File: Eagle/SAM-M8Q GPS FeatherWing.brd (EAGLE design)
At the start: 50.8 x 22.9 mm, 25 parts, among them Q1 DMG3415U-7, Q2 2N2222, SW1 KMR2, U1 SAM-M8Q

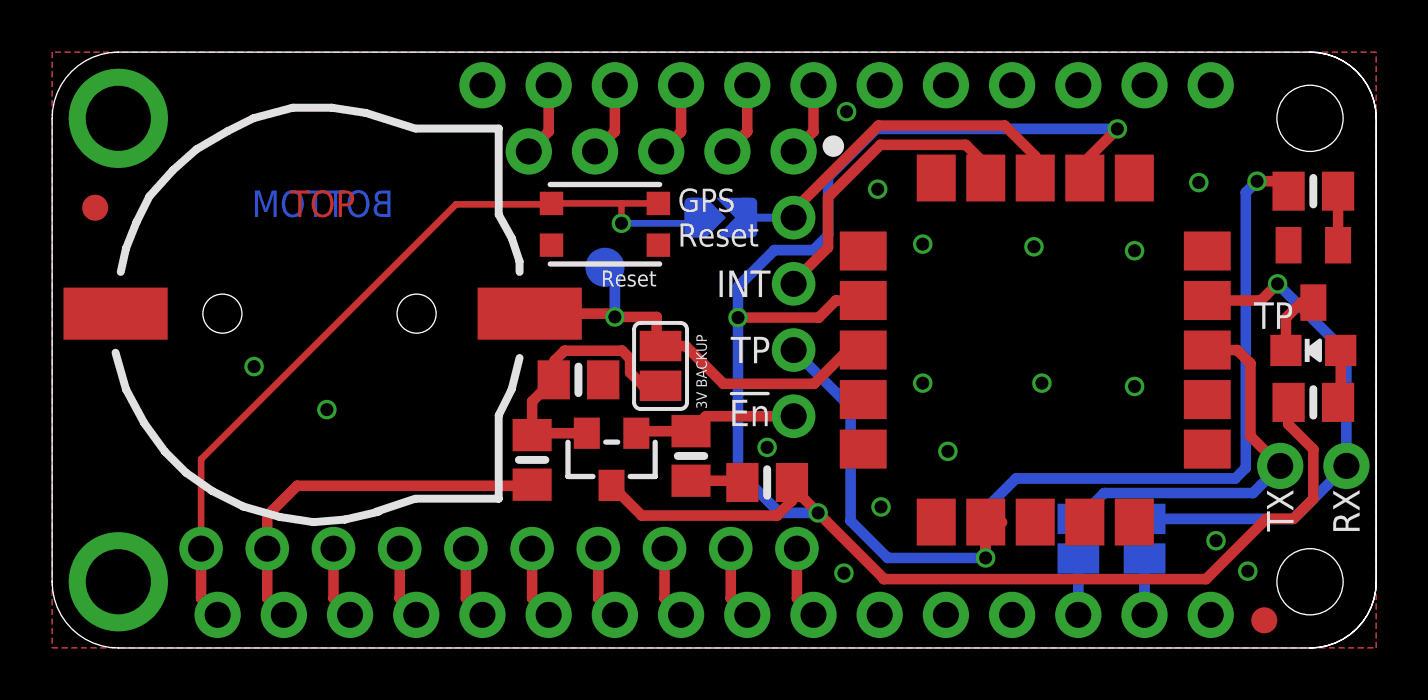
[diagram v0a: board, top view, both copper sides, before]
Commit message: Reduced vias. Added pad for SAFEBOOT.
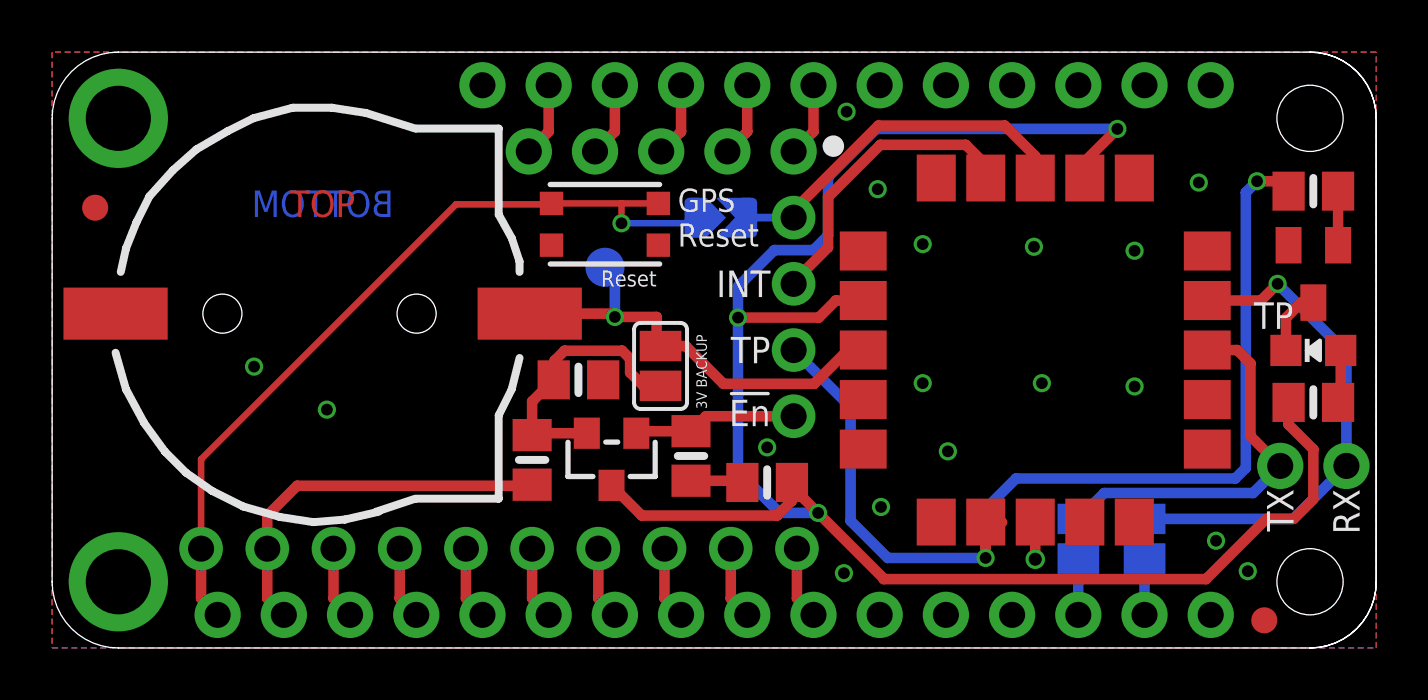
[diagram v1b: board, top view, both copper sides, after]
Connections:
- new net SAFEBOOT: U1.8
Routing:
- net SAFEBOOT: track 0.00 -> 1.43 mm, vias 0 -> 1
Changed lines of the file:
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@@
 <text x="38.1" y="18.034" size="1.6764" layer="22" font="vector" ratio="15" rot="MR0" align="center">SAM-M8Q GPS
 FeatherWing</text>
-<text x="43.688" y="4.191" size="1.016" layer="22" font="vector" ratio="14" rot="MR270" align="center">RX</text>
-<text x="37.465" y="4.191" size="1.016" layer="22" font="vector" ratio="14" rot="MR270" align="center">TX</text>
+<text x="43.7134" y="4.953" size="1.016" layer="22" font="vector" ratio="14" rot="MR270" align="center">RX</text>
+<text x="37.5666" y="4.953" size="1.016" layer="22" font="vector" ratio="14" rot="MR270" align="center">TX</text>
 <text x="13.2588" y="5.3594" size="1.016" layer="22" font="vector" ratio="14" rot="MR180" align="center">GND</text>
 <text x="5.4864" y="5.3848" size="1.016" layer="22" font="vector" ratio="14" rot="MR0" align="center">RST</text>
@@
 <text x="47.625" y="13.2588" size="1.016" layer="21" ratio="13" rot="R180">TP</text>
 <circle x="29.972" y="19.2532" radius="0.209453125" width="0.4064" layer="21"/>
-<text x="25.1206" y="9.1694" size="0.4064" layer="21" ratio="15" rot="R90">3V BACKUP</text>
+<text x="25.1206" y="9.1694" size="0.4064" layer="21" ratio="18" rot="R90">3V BACKUP</text>
 <text x="9.1186" y="16.5354" size="1.016" layer="1" ratio="15">TOP</text>
 <text x="13.1064" y="16.5354" size="1.016" layer="16" ratio="15" rot="MR0">BOTTOM</text>
@@
 <contactref element="JP4" pad="7"/>
 <contactref element="R2" pad="1"/>
-<via x="7.747" y="10.795" extent="1-16" drill="0.5"/>
-<via x="10.541" y="9.144" extent="1-16" drill="0.5"/>
+<via x="7.747" y="10.795" extent="1-16" drill="0.45"/>
+<via x="10.541" y="9.144" extent="1-16" drill="0.45"/>
 <contactref element="U1" pad="4"/>
 <contactref element="U1" pad="10"/>
@@
 <wire x1="26.416" y1="6.416" x2="24.511" y2="6.416" width="0.4064" layer="1"/>
 <contactref element="Q2" pad="E"/>
-<via x="27.432" y="7.6962" extent="1-16" drill="0.5"/>
-<via x="31.6738" y="17.6022" extent="1-16" drill="0.5"/>
-<via x="31.8008" y="5.4102" extent="1-16" drill="0.5"/>
-<via x="37.973" y="10.16" extent="1-16" drill="0.5"/>
-<via x="41.529" y="15.24" extent="1-16" drill="0.5"/>
-<via x="45.8724" y="2.9464" extent="1-16" drill="0.5"/>
-<via x="33.401" y="15.494" extent="1-16" drill="0.5"/>
-<via x="37.6682" y="15.3924" extent="1-16" drill="0.5"/>
-<via x="33.401" y="10.16" extent="1-16" drill="0.5"/>
-<via x="43.9928" y="17.8562" extent="1-16" drill="0.5"/>
-<via x="41.529" y="10.033" extent="1-16" drill="0.5"/>
-<via x="44.6532" y="4.1148" extent="1-16" drill="0.5"/>
-<via x="30.3784" y="2.8702" extent="1-16" drill="0.5"/>
-<via x="30.48" y="20.574" extent="1-16" drill="0.5"/>
-<via x="34.3662" y="7.5438" extent="1-16" drill="0.5"/>
+<via x="27.432" y="7.6962" extent="1-16" drill="0.45"/>
+<via x="31.6738" y="17.6022" extent="1-16" drill="0.45"/>
+<via x="31.8008" y="5.4102" extent="1-16" drill="0.45"/>
+<via x="37.973" y="10.16" extent="1-16" drill="0.45"/>
+<via x="41.529" y="15.24" extent="1-16" drill="0.45"/>
+<via x="45.8724" y="2.9464" extent="1-16" drill="0.45"/>
+<via x="33.401" y="15.494" extent="1-16" drill="0.45"/>
+<via x="37.6682" y="15.3924" extent="1-16" drill="0.45"/>
+<via x="33.401" y="10.16" extent="1-16" drill="0.45"/>
+<via x="43.9928" y="17.8562" extent="1-16" drill="0.45"/>
+<via x="41.529" y="10.033" extent="1-16" drill="0.45"/>
+<via x="44.6532" y="4.1148" extent="1-16" drill="0.45"/>
+<via x="30.3784" y="2.8702" extent="1-16" drill="0.45"/>
+<via x="30.48" y="20.574" extent="1-16" drill="0.45"/>
+<via x="34.3662" y="7.5438" extent="1-16" drill="0.45"/>
 </signal>
 <signal name="3.3V">
@@
 <wire x1="18.323" y1="12.827" x2="21.463" y2="12.827" width="0.4064" layer="1"/>
 <wire x1="21.463" y1="12.827" x2="21.59" y2="12.7" width="0.4064" layer="1"/>
-<via x="21.59" y="12.7" extent="1-16" drill="0.5"/>
+<via x="21.59" y="12.7" extent="1-16" drill="0.45"/>
 <contactref element="TP1" pad="P$1"/>
 <contactref element="U1" pad="3"/>
@@
 <wire x1="47.625" y1="4.953" x2="49.657" y2="6.985" width="0.4064" layer="16"/>
 <wire x1="49.657" y1="6.985" x2="49.657" y2="11.3284" width="0.4064" layer="16"/>
-<via x="47.0154" y="13.97" extent="1-16" drill="0.5"/>
+<via x="47.0154" y="13.97" extent="1-16" drill="0.45"/>
 <wire x1="46.3754" y1="13.33" x2="44.319" y2="13.33" width="0.4064" layer="1"/>
 <wire x1="49.657" y1="11.3284" x2="47.0154" y2="13.97" width="0.4064" layer="16"/>
@@
 <wire x1="35.819" y1="4.83" x2="35.814" y2="4.83" width="0.4064" layer="1"/>
 <wire x1="35.814" y1="4.83" x2="35.814" y2="3.4544" width="0.4064" layer="1"/>
-<via x="35.814" y="3.4544" extent="1-16" drill="0.5"/>
-<via x="46.228" y="17.907" extent="1-16" drill="0.5"/>
+<via x="35.814" y="3.4544" extent="1-16" drill="0.45"/>
+<via x="46.228" y="17.907" extent="1-16" drill="0.45"/>
 <wire x1="46.228" y1="17.907" x2="47.056" y2="17.907" width="0.4064" layer="1"/>
 <wire x1="47.056" y1="17.907" x2="47.437" y2="17.526" width="0.4064" layer="1"/>
@@
 <wire x1="15.494" y1="17.018" x2="19.121" y2="17.018" width="0.254" layer="1"/>
 <wire x1="19.121" y1="17.018" x2="19.159" y2="17.056" width="0.254" layer="1"/>
-<via x="21.844" y="16.294" extent="1-16" drill="0.5"/>
+<via x="21.844" y="16.294" extent="1-16" drill="0.45"/>
 <wire x1="19.159" y1="17.056" x2="21.844" y2="17.056" width="0.254" layer="1"/>
 <wire x1="21.844" y1="17.056" x2="23.259" y2="17.056" width="0.254" layer="1"/>
@@
 <wire x1="46.5836" y1="4.953" x2="44.2722" y2="2.6416" width="0.4064" layer="1"/>
 <wire x1="44.2722" y1="2.6416" x2="31.9024" y2="2.6416" width="0.4064" layer="1"/>
-<via x="29.3878" y="5.1816" extent="1-16" drill="0.5"/>
+<via x="29.3878" y="5.1816" extent="1-16" drill="0.45"/>
 <wire x1="31.9024" y1="2.6416" x2="31.9024" y2="2.667" width="0.4064" layer="1"/>
 <wire x1="31.9024" y1="2.667" x2="29.3878" y2="5.1816" width="0.4064" layer="1"/>
@@
 <wire x1="27.9146" y1="5.1816" x2="26.3144" y2="6.7818" width="0.4064" layer="16"/>
 <wire x1="26.3144" y1="6.7818" x2="26.3144" y2="12.6746" width="0.4064" layer="16"/>
-<via x="26.3144" y="12.6746" extent="1-16" drill="0.5"/>
+<via x="26.3144" y="12.6746" extent="1-16" drill="0.45"/>
 <wire x1="26.3144" y1="12.6746" x2="29.4132" y2="12.6746" width="0.4064" layer="1"/>
 <wire x1="29.4132" y1="12.6746" x2="30.0686" y2="13.33" width="0.4064" layer="1"/>
@@
 <wire x1="39.619" y1="18.03" x2="39.619" y2="18.664" width="0.4064" layer="1"/>
 <wire x1="39.619" y1="18.664" x2="40.8686" y2="19.9136" width="0.4064" layer="1"/>
-<via x="40.8686" y="19.9136" extent="1-16" drill="0.5"/>
+<via x="40.8686" y="19.9136" extent="1-16" drill="0.45"/>
 <wire x1="40.8686" y1="19.9136" x2="31.623" y2="19.9136" width="0.4064" layer="16"/>
 <wire x1="31.623" y1="19.9136" x2="29.7688" y2="18.0594" width="0.4064" layer="16"/>
@@
 <wire x1="49.337" y1="15.451" x2="49.337" y2="17.526" width="0.4064" layer="1"/>
 </signal>
+<signal name="SAFEBOOT">
+<contactref element="U1" pad="8"/>
+<via x="37.719" y="3.4036" extent="1-16" drill="0.5" shape="square"/>
+<wire x1="37.719" y1="4.83" x2="37.719" y2="3.4036" width="0.4064" layer="1"/>
+</signal>
 </signals>

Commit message: Added a test pad for safeboot
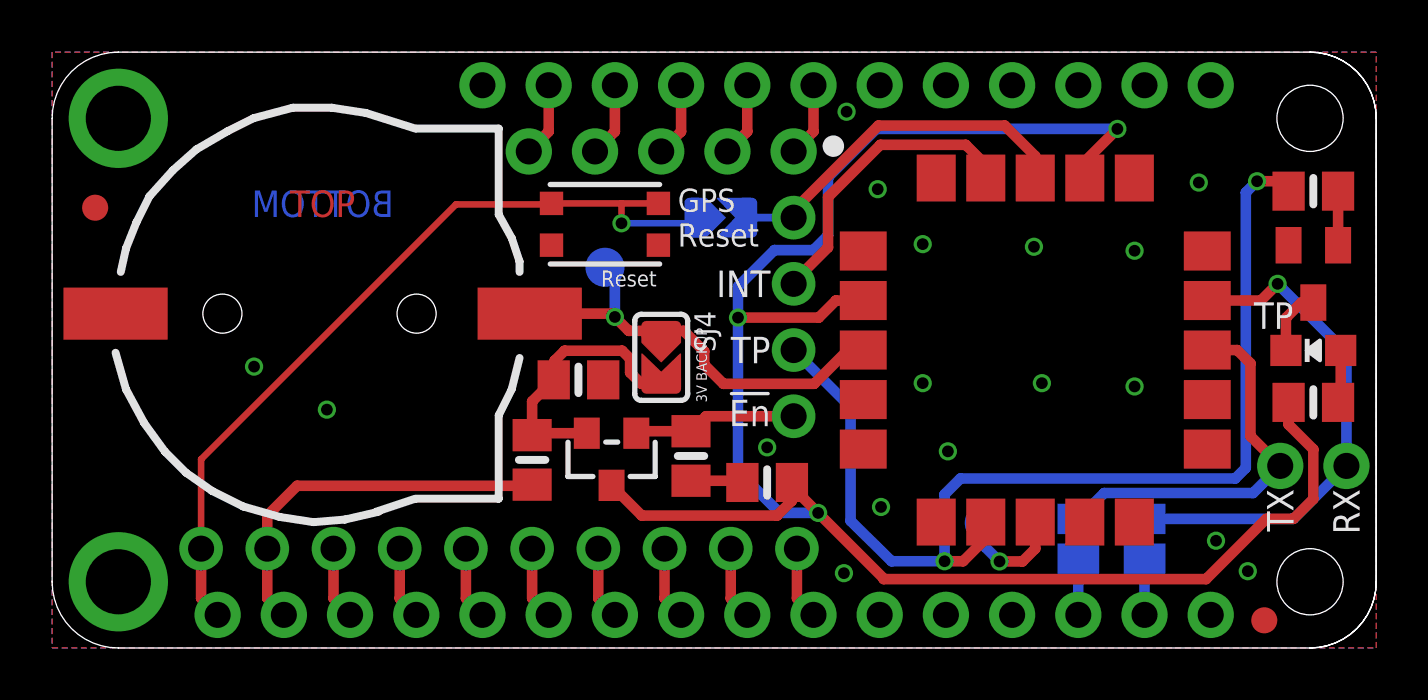
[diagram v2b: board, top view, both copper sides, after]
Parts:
- added TP2: (no value), microbuilder:TESTPOINT_ROUND_1.5MM
- SJ4: device jumper:SJ -> microbuilder:SOLDERJUMPER_ARROW_NOPASTE
- moved SJ4 0.33 mm to (23.4, 11.2)
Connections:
- net SAFEBOOT: now also TP2.P$1
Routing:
- net SAFEBOOT: track 1.43 -> 4.32 mm
- net TP: track 40.3 -> 41.4 mm
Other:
- board text added: "SAFEBOOT"
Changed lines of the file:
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@@
 <?xml version="1.0" encoding="utf-8"?>
 <!DOCTYPE eagle SYSTEM "eagle.dtd">
-<eagle version="8.2.2">
+<eagle version="8.3.2">
 <drawing>
 <settings>
 <setting alwaysvectorfont="yes"/>
+<setting keepoldvectorfont="yes"/>
 <setting verticaltext="up"/>
 </settings>
@@
 <text x="38.1" y="18.034" size="1.6764" layer="22" font="vector" ratio="15" rot="MR0" align="center">SAM-M8Q GPS
 FeatherWing</text>
-<text x="43.7134" y="4.953" size="1.016" layer="22" font="vector" ratio="14" rot="MR270" align="center">RX</text>
-<text x="37.5666" y="4.953" size="1.016" layer="22" font="vector" ratio="14" rot="MR270" align="center">TX</text>
+<text x="43.6372" y="4.2164" size="1.016" layer="22" font="vector" ratio="14" rot="MR270" align="center">RX</text>
+<text x="37.592" y="4.1656" size="1.016" layer="22" font="vector" ratio="14" rot="MR270" align="center">TX</text>
 <text x="13.2588" y="5.3594" size="1.016" layer="22" font="vector" ratio="14" rot="MR180" align="center">GND</text>
 <text x="5.4864" y="5.3848" size="1.016" layer="22" font="vector" ratio="14" rot="MR0" align="center">RST</text>
@@
 <text x="47.625" y="13.2588" size="1.016" layer="21" ratio="13" rot="R180">TP</text>
 <circle x="29.972" y="19.2532" radius="0.209453125" width="0.4064" layer="21"/>
-<text x="25.1206" y="9.1694" size="0.4064" layer="21" ratio="18" rot="R90">3V BACKUP</text>
+<text x="25.1206" y="9.4234" size="0.4064" layer="21" ratio="18" rot="R90">3V BACKUP</text>
 <text x="9.1186" y="16.5354" size="1.016" layer="1" ratio="15">TOP</text>
 <text x="13.1064" y="16.5354" size="1.016" layer="16" ratio="15" rot="MR0">BOTTOM</text>
@@
 <circle x="1.651" y="16.891" radius="0.499871875" width="0" layer="31"/>
 <circle x="46.505" y="1.061" radius="0.499871875" width="0" layer="31"/>
+<text x="32.1818" y="4.5212" size="0.6096" layer="22" ratio="15" rot="MR180" align="center">SAFEBOOT</text>
 </plain>
 <attributes>
@@
 <element name="Q2" library="transistor" package="SOT23-BEC" value="2N2222" x="48.387" y="14.351" smashed="yes" rot="R180"/>
 <element name="R3" library="microbuilder" package="0805-NO" value="1K" x="48.387" y="17.526" smashed="yes"/>
-<element name="SJ4" library="jumper" package="SJ" value="" x="23.3426" y="10.8204" smashed="yes" rot="R270">
-<attribute name="VALUE" x="23.3426" y="10.4203" size="0.02" layer="27" rot="R270"/>
+<element name="TP2" library="microbuilder" package="TESTPOINT_ROUND_1.5MM" value="" x="35.7632" y="4.8006" smashed="yes" rot="MR0">
+<attribute name="VALUE" x="34.6202" y="4.1656" size="0.4064" layer="28" ratio="10" rot="MR0"/>
+</element>
+<element name="SJ4" library="microbuilder" package="SOLDERJUMPER_ARROW_NOPASTE" value="" x="23.368" y="11.1506" rot="R270">
+<attribute name="BOM" value="EXCLUDE" x="23.368" y="11.1506" size="0.0508" layer="27" rot="R270" display="off"/>
 </element>
 </elements>
@@
 <wire x1="19.243" y1="10.287" x2="18.415" y2="9.459" width="0.4064" layer="1"/>
 <wire x1="18.415" y1="9.459" x2="18.415" y2="8.165" width="0.4064" layer="1"/>
-<contactref element="SJ4" pad="2"/>
-<wire x1="23.3426" y1="10.0584" x2="22.6822" y2="10.0584" width="0.4064" layer="1"/>
-<wire x1="22.6822" y1="10.0584" x2="22.1742" y2="10.5664" width="0.4064" layer="1"/>
-<wire x1="22.1742" y1="10.5664" x2="22.1742" y2="11.0998" width="0.4064" layer="1"/>
+<wire x1="22.1742" y1="11.0998" x2="22.1742" y2="10.5664" width="0.4064" layer="1"/>
 <wire x1="22.1742" y1="11.0998" x2="21.8694" y2="11.4046" width="0.4064" layer="1"/>
 <wire x1="21.8694" y1="11.4046" x2="19.6596" y2="11.4046" width="0.4064" layer="1"/>
@@
 <wire x1="19.2786" y1="11.0236" x2="19.2786" y2="10.3226" width="0.4064" layer="1"/>
 <wire x1="19.2786" y1="10.3226" x2="19.243" y2="10.287" width="0.4064" layer="1"/>
+<contactref element="SJ4" pad="2"/>
+<wire x1="22.1742" y1="10.5664" x2="22.606" y2="10.1346" width="0.4064" layer="1"/>
+<wire x1="22.606" y1="10.1346" x2="23.368" y2="10.1346" width="0.4064" layer="1"/>
 </signal>
 <signal name="VBACKUP">
@@
 <wire x1="21.59" y1="12.7" x2="21.59" y2="14.224" width="0.4064" layer="16"/>
 <wire x1="21.59" y1="14.224" x2="21.209" y2="14.605" width="0.4064" layer="16"/>
-<wire x1="23.1902" y1="12.7" x2="21.59" y2="12.7" width="0.4064" layer="1"/>
-<wire x1="25.7556" y1="10.1346" x2="29.2354" y2="10.1346" width="0.4064" layer="1"/>
+<wire x1="29.2354" y1="10.1346" x2="25.7556" y2="10.1346" width="0.4064" layer="1"/>
 <wire x1="29.2354" y1="10.1346" x2="30.5308" y2="11.43" width="0.4064" layer="1"/>
 <wire x1="30.5308" y1="11.43" x2="31.119" y2="11.43" width="0.4064" layer="1"/>
 <contactref element="SJ4" pad="1"/>
-<wire x1="23.1902" y1="12.7" x2="23.1902" y2="11.7348" width="0.4064" layer="1"/>
-<wire x1="23.1902" y1="11.7348" x2="23.3426" y2="11.5824" width="0.4064" layer="1"/>
-<wire x1="25.7556" y1="10.1346" x2="24.3078" y2="11.5824" width="0.4064" layer="1"/>
-<wire x1="24.3078" y1="11.5824" x2="23.3426" y2="11.5824" width="0.4064" layer="1"/>
+<wire x1="25.7556" y1="10.1346" x2="25.019" y2="10.8712" width="0.4064" layer="1"/>
+<wire x1="25.019" y1="10.8712" x2="25.019" y2="11.3792" width="0.4064" layer="1"/>
+<wire x1="25.019" y1="11.3792" x2="24.2316" y2="12.1666" width="0.4064" layer="1"/>
+<wire x1="23.368" y1="12.1666" x2="24.2316" y2="12.1666" width="0.4064" layer="1"/>
+<wire x1="21.59" y1="12.7" x2="22.1234" y2="12.1666" width="0.4064" layer="1"/>
+<wire x1="22.1234" y1="12.1666" x2="23.368" y2="12.1666" width="0.4064" layer="1"/>
 </signal>
 <signal name="TX">
@@
 <contactref element="JP1" pad="3"/>
 <contactref element="U1" pad="7"/>
-<wire x1="36.449" y1="4.825" x2="35.819" y2="4.83" width="0.4064" layer="1"/>
 <contactref element="R3" pad="1"/>
-<wire x1="35.819" y1="4.83" x2="35.814" y2="4.83" width="0.4064" layer="1"/>
-<wire x1="35.814" y1="4.83" x2="35.814" y2="3.4544" width="0.4064" layer="1"/>
-<via x="35.814" y="3.4544" extent="1-16" drill="0.45"/>
+<via x="34.2392" y="3.3274" extent="1-16" drill="0.45"/>
 <via x="46.228" y="17.907" extent="1-16" drill="0.45"/>
 <wire x1="46.228" y1="17.907" x2="47.056" y2="17.907" width="0.4064" layer="1"/>
 <wire x1="47.056" y1="17.907" x2="47.437" y2="17.526" width="0.4064" layer="1"/>
-<wire x1="35.814" y1="3.4544" x2="35.814" y2="5.334" width="0.4064" layer="16"/>
-<wire x1="35.814" y1="5.334" x2="36.9824" y2="6.5024" width="0.4064" layer="16"/>
-<wire x1="36.9824" y1="6.5024" x2="45.3898" y2="6.5024" width="0.4064" layer="16"/>
+<wire x1="34.2392" y1="3.3274" x2="34.2392" y2="5.8928" width="0.4064" layer="16"/>
+<wire x1="34.2392" y1="5.8928" x2="34.8488" y2="6.5024" width="0.4064" layer="16"/>
+<wire x1="34.8488" y1="6.5024" x2="45.3898" y2="6.5024" width="0.4064" layer="16"/>
 <wire x1="45.3898" y1="6.5024" x2="45.7962" y2="6.9088" width="0.4064" layer="16"/>
 <wire x1="45.7962" y1="6.9088" x2="45.7962" y2="17.4752" width="0.4064" layer="16"/>
@@
 <wire x1="28.448" y1="11.43" x2="30.6324" y2="9.2456" width="0.4064" layer="16"/>
 <wire x1="30.6324" y1="9.2456" x2="30.6324" y2="4.8768" width="0.4064" layer="16"/>
-<wire x1="30.6324" y1="4.8768" x2="32.0548" y2="3.4544" width="0.4064" layer="16"/>
-<wire x1="32.0548" y1="3.4544" x2="35.814" y2="3.4544" width="0.4064" layer="16"/>
+<wire x1="30.6324" y1="4.8768" x2="32.2072" y2="3.3274" width="0.4064" layer="16"/>
+<wire x1="32.2072" y1="3.3274" x2="34.2392" y2="3.3274" width="0.4064" layer="16"/>
+<wire x1="35.819" y1="4.83" x2="35.819" y2="4.196" width="0.4064" layer="1"/>
+<wire x1="34.9504" y1="3.3274" x2="34.2392" y2="3.3274" width="0.4064" layer="1"/>
+<wire x1="35.819" y1="4.196" x2="34.9504" y2="3.3274" width="0.4064" layer="1"/>
 </signal>
 <signal name="3V">
@@
 <signal name="SAFEBOOT">
 <contactref element="U1" pad="8"/>
-<via x="37.719" y="3.4036" extent="1-16" drill="0.5" shape="square"/>
-<wire x1="37.719" y1="4.83" x2="37.719" y2="3.4036" width="0.4064" layer="1"/>
+<contactref element="TP2" pad="P$1"/>
+<wire x1="37.719" y1="4.83" x2="37.719" y2="3.81" width="0.4064" layer="1"/>
+<wire x1="37.2288" y1="3.3198" x2="36.3474" y2="3.3198" width="0.4064" layer="1"/>
+<via x="36.3474" y="3.3198" extent="1-16" drill="0.45"/>
+<wire x1="36.3474" y1="3.3198" x2="35.7632" y2="3.904" width="0.4064" layer="16"/>
+<wire x1="35.7632" y1="3.904" x2="35.7632" y2="4.8006" width="0.4064" layer="16"/>
+<wire x1="37.719" y1="3.81" x2="37.2288" y2="3.3198" width="0.4064" layer="1"/>
 </signal>
 </signals>
